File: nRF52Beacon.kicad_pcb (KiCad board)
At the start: 2 copper layers, 25.4 x 27.9 mm, 106 parts, among them P1 CONN_01X06, U1 nRF52832-QFAA, Y1 32.768kHz, Y2 32MHz

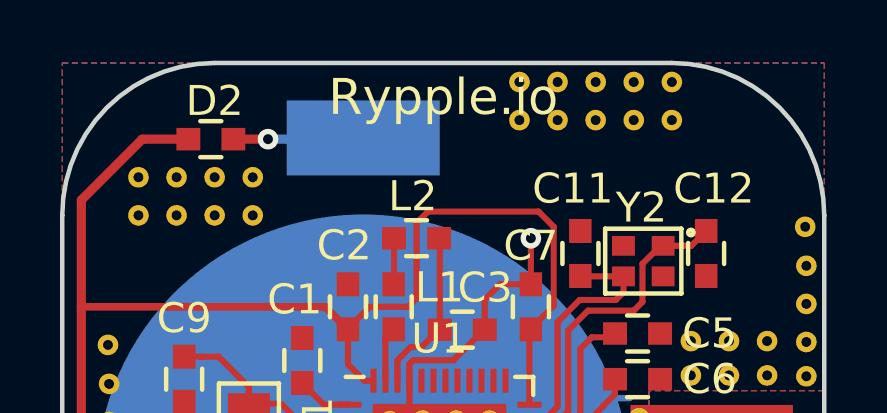
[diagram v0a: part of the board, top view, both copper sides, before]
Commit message: Removed paste from TC2030 pads
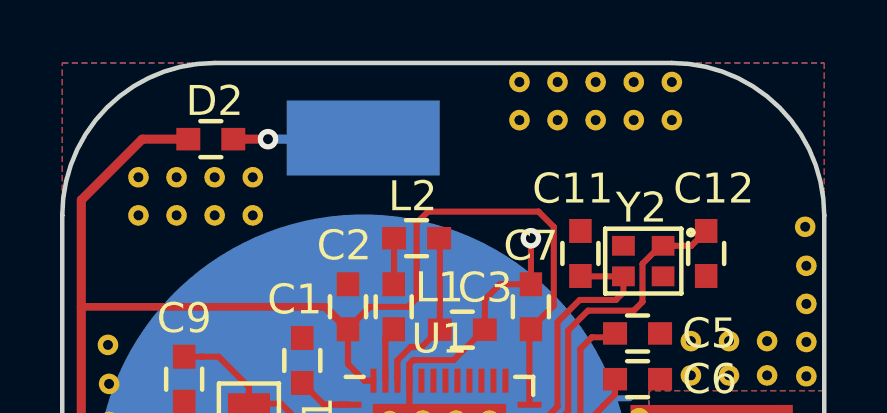
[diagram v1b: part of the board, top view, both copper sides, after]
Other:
- board text removed: "Rypple.io"
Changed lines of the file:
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@@
 (kicad_pcb (version 4) (host pcbnew 4.0.2-stable)
   (general
-    (links 153)
-    (no_connects 3)
+    (links 162)
+    (no_connects 1)
     (area 149.585458 96.8396 181.432358 131.338542)
     (thickness 1.6)
-    (drawings 10)
+    (drawings 9)
     (tracks 184)
     (zones 0)
@@
     (add_net VDD)
   )
+  (module New_Footprints:TC2030-MCP-NL (layer F.Cu)
+    (at 169.926 121.92 270)
+    (fp_text reference P1 (at 2.54 2.032 360) (layer F.SilkS)
+      (effects (font (size 1 1) (thickness 0.15)))
+    )
+    (fp_text value CONN_01X06 (at 0 -3.6 270) (layer F.Fab)
+      (effects (font (size 1 1) (thickness 0.15)))
+    )
+    (pad "" np_thru_hole circle (at 0 0 270) (size 1 1) (drill 1) (layers *.Cu *.Mask F.SilkS)
+      (solder_mask_margin 0.05))
+    (pad "" np_thru_hole circle (at 5.08 -1.016 270) (size 1 1) (drill 1) (layers *.Cu *.Mask F.SilkS)
+      (solder_mask_margin 0.05))
+    (pad "" np_thru_hole circle (at 5.08 1.016 270) (size 1 1) (drill 1) (layers *.Cu *.Mask F.SilkS)
+      (solder_mask_margin 0.05))
+    (pad 1 smd circle (at 1.27 0.635 270) (size 0.787 0.787) (layers F.Cu F.Mask)
+      (net 3 VDD) (solder_mask_margin 0.05))
+    (pad 2 smd circle (at 1.27 -0.635 270) (size 0.787 0.787) (layers F.Cu F.Mask)
+      (net 34 /SWDIO) (solder_mask_margin 0.05))
+    (pad 3 smd circle (at 2.54 0.635 270) (size 0.787 0.787) (layers F.Cu F.Mask)
+      (net 32 /nRESET) (solder_mask_margin 0.05))
+    (pad 4 smd circle (at 2.54 -0.635 270) (size 0.787 0.787) (layers F.Cu F.Mask)
+      (net 33 /SWDCLK) (solder_mask_margin 0.05))
+    (pad 5 smd circle (at 3.81 0.635 270) (size 0.787 0.787) (layers F.Cu F.Mask)
+      (net 2 GND) (solder_mask_margin 0.05))
+    (pad 6 smd circle (at 3.81 -0.635 270) (size 0.787 0.787) (layers F.Cu F.Mask)
+      (net 46 /SWO) (solder_mask_margin 0.05))
+  )
   (module New_Footprints:BATT-HLD-001 (layer B.Cu)
     (at 162.433 114.28 90)
@@
     (pad 1 thru_hole circle (at 0 0) (size 0.6858 0.6858) (drill 0.3302) (layers *.Cu)
       (net 2 GND) (zone_connect 2))
-  )
-  (module New_Footprints:TC2030-MCP-NL (layer F.Cu)
-    (at 169.926 121.92 270)
-    (fp_text reference P1 (at 2.54 2.032 360) (layer F.SilkS)
-      (effects (font (size 1 1) (thickness 0.15)))
-    )
-    (fp_text value CONN_01X06 (at 0 -3.6 270) (layer F.Fab)
-      (effects (font (size 1 1) (thickness 0.15)))
-    )
-    (pad "" np_thru_hole circle (at 0 0 270) (size 1 1) (drill 1) (layers *.Cu *.Mask F.SilkS)
-      (solder_mask_margin 0.05))
-    (pad "" np_thru_hole circle (at 5.08 -1.016 270) (size 1 1) (drill 1) (layers *.Cu *.Mask F.SilkS)
-      (solder_mask_margin 0.05))
-    (pad "" np_thru_hole circle (at 5.08 1.016 270) (size 1 1) (drill 1) (layers *.Cu *.Mask F.SilkS)
-      (solder_mask_margin 0.05))
-    (pad 1 smd circle (at 1.27 0.635 270) (size 0.787 0.787) (layers F.Cu F.Paste F.Mask)
-      (net 3 VDD) (solder_mask_margin 0.05))
-    (pad 2 smd circle (at 1.27 -0.635 270) (size 0.787 0.787) (layers F.Cu F.Paste F.Mask)
-      (net 34 /SWDIO) (solder_mask_margin 0.05))
-    (pad 3 smd circle (at 2.54 0.635 270) (size 0.787 0.787) (layers F.Cu F.Paste F.Mask)
-      (net 32 /nRESET) (solder_mask_margin 0.05))
-    (pad 4 smd circle (at 2.54 -0.635 270) (size 0.787 0.787) (layers F.Cu F.Paste F.Mask)
-      (net 33 /SWDCLK) (solder_mask_margin 0.05))
-    (pad 5 smd circle (at 3.81 0.635 270) (size 0.787 0.787) (layers F.Cu F.Paste F.Mask)
-      (net 2 GND) (solder_mask_margin 0.05))
-    (pad 6 smd circle (at 3.81 -0.635 270) (size 0.787 0.787) (layers F.Cu F.Paste F.Mask)
-      (net 46 /SWO) (solder_mask_margin 0.05))
   )
   (module Capacitors_SMD:C_0603 (layer F.Cu)
@@
       (net 12 /RF_OUT))
   )
-  (gr_text Rypple.io (at 165.1 101.473) (layer F.SilkS)
-    (effects (font (size 1.2 1.2) (thickness 0.2)))
-  )
   (gr_text "nRF52\nBeaconBuddy" (at 161.544 125.984) (layer F.SilkS)
